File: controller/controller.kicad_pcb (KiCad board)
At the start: 2 copper layers, 241 parts, among them J1 CONN_01X10, J2 CONN_01X10, J3 CONN_01X10, J4 CONN_01X10, K1 RELAY_SEPARATED, K10 RELAY_SEPARATED, K11 RELAY_SEPARATED, K12 RELAY_SEPARATED, K13 RELAY_SEPARATED, K14 RELAY_SEPARATED, K15 RELAY_SEPARATED, K16 RELAY_SEPARATED, K17 RELAY_SEPARATED, K18 RELAY_SEPARATED, K19 RELAY_SEPARATED, K2 RELAY_SEPARATED, K20 RELAY_SEPARATED, K21 RELAY_SEPARATED, K22 RELAY_SEPARATED, K23 RELAY_SEPARATED, K24 RELAY_SEPARATED, K25 RELAY_SEPARATED, K26 RELAY_SEPARATED, K3 RELAY_SEPARATED, K4 RELAY_SEPARATED, K5 RELAY_SEPARATED, K6 RELAY_SEPARATED, K7 RELAY_SEPARATED, K8 RELAY_SEPARATED, K9 RELAY_SEPARATED, Q1 Q_NMOS_GSD, Q2 Q_NMOS_GSD, Q3 Q_PMOS_GSD, Q4 Q_NMOS_GSD, Q5 Q_PMOS_GSD, Q6 Q_PMOS_GSD, Q7 Q_NMOS_GSD, Q8 NDT2955, Q9 Q_NMOS_GSD, U1 OPTO-TRANSISTOR-4, U10 ULN2803A, U11 ULN2803A, U12 OPTO-TRANSISTOR-4, U2 ULN2801A, U3 SN65HVD72, U5 LM7805CT, U6 ULN2801A, U7 74LS04, U8 VNH3SP30, U9 74HC595

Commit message: Finish the routing, add some significant fixes: *correct to-252 pin numbering * longer pads for relays * fix footprint of the optocouplers
Also finish the routing
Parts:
- removed D40, D41: LED_Small_ALT, LEDs:LED_D5.0mm
- removed R27, R31, R32: R, Resistors_SMD:R_0603_HandSoldering
- added C45: 1u, Capacitors_SMD:C_0603_HandSoldering, B.Cu at (116.0, 95.0)
- added C46: C, Capacitors_SMD:C_0603_HandSoldering, B.Cu at (198.3, 130.1)
- added C47: 1u, Capacitors_SMD:C_1210_HandSoldering, B.Cu at (214.0, 143.5)
- added C48: 1u, Capacitors_SMD:C_0603, B.Cu at (145.2, 138.5)
- added J21: CONN_01X04, Connectors_JST:JST_EH_B04B-EH-A_04x2.50mm_Straight, F.Cu at (85.9, 159.6)
- added J22: BATT, Connectors_Terminal_Blocks:TerminalBlock_Pheonix_MKDS1.5-2pol, F.Cu at (65.4, 159.1)
- added J23: CONN_01X02, Connectors_Terminal_Blocks:TerminalBlock_Pheonix_MKDS1.5-2pol, F.Cu at (115.4, 157.6)
- added J24: CONN_01X02, Connectors_Terminal_Blocks:TerminalBlock_Pheonix_MKDS1.5-2pol, F.Cu at (273.9, 134.6)
- added J5: CONN_01X02, Connectors_Terminal_Blocks:TerminalBlock_Pheonix_MKDS1.5-2pol, F.Cu at (274.2, 151.2)
- added J6: CONN_01X05, Connectors_Terminal_Blocks:TerminalBlock_Pheonix_MKDS1.5-5pol, F.Cu at (145.4, 158.6)
- added J7: CONN_01X06, Socket_Strips:Socket_Strip_Straight_1x06_Pitch2.54mm, F.Cu at (147.9, 138.0)
- added R20: 0R05, TO_SOT_Packages_THT:TO-220-2_Vertical, F.Cu at (231.5, 144.5)
- added TP1: TEST, Measurement_Points:Measurement_Point_Round-TH_Small, F.Cu at (273.4, 94.1)
- added U13: LTV-814, Housings_DIP:DIP-4_W11.48mm_SMD, B.Cu at (265.5, 79.5)
- added U14: LTV-814, Housings_DIP:DIP-4_W11.48mm_SMD, B.Cu at (265.5, 98.6)
- added U15: LTV-814, Housings_DIP:DIP-4_W11.48mm_SMD, B.Cu at (265.5, 104.6)
- added U16: LM7805CT, TO_SOT_Packages_THT:TO-220_Vertical, F.Cu at (44.5, 116.5)
- added U4: LTV-814, Housings_DIP:DIP-4_W11.48mm_SMD, B.Cu at (245.9, 79.6)
- C16, C8: value C -> 1u
- C20, C21, C33, C35, C36, C38, C39, D16, D28, D34, D52, D53, D54, D56, D57, D58, Q1, Q2, Q3, Q4, Q5, Q6, Q7, Q8, Q9, R1, R10, R11, R12, R13, R14, R15, R16, R17, R18, R19, R2, R21, R22, R23, R24, R25, R26, R28, R29, R3, R30, R33, R4, R42, R43, R44, R45, R46, R47, R48, R49, R5, R50, R51, R52, R53, R54, R55, R56, R57, R58, R59, R6, R61, R62, R63, R64, R65, R66, R67, R68, R7, R8, R9, U3, U5, U8: moved to B.Cu
- C44: value C -> 1u; moved to B.Cu
- D30, D31, D32, D33, D51: footprint LEDs:LED_0805 -> LEDs:LED_D5.0mm
- D36: value LED_Small_ALT -> 5V; footprint LEDs:LED_D5.0mm -> Diodes_SMD:SOD-123; moved to B.Cu
- D55: footprint LEDs:LED_0603 -> LEDs:LED_D5.0mm
- J1, J2, J3, J4: footprint Connectors_Terminal_Blocks:TerminalBlock_Pheonix_MKDS1.5-10pol -> smalsiukas-footpints:TerminalBlock_5.08-10pol
- R60: footprint Resistors_SMD:R_0603 -> Resistors_SMD:R_0603_HandSoldering; moved to B.Cu
- RN1: value R_Network08 -> R_Pack08; footprint Resistors_THT:R_Array_SIP9 -> Resistors_SMD:R_Array_Convex_8x0602; moved to B.Cu
- RV1, RV2, RV3, RV4, RV5, RV6, RV7: footprint Potentiometers:Potentiometer_Trimmer_Bourns_3296P -> Potentiometers:Potentiometer_Trimmer_Bourns_3296W
- SH1: footprint w_conn_misc:arduino_nano_header -> SHIELD_ARDUINO:ARDUINO_NANO_2_CONTOUR_ELL
- U1, U12: value OPTO-TRANSISTOR-4 -> LTV-814; moved to B.Cu
- U7: value 74LS04 -> SN74AHCT1G14DBVR; moved to B.Cu
- U9: value 74HC595 -> 74HC595_WITH_PWR
- moved MK8 225.6 mm to (44.9, 43.6)
- moved R60 204.3 mm to (48.4, 138.1), turned to 90 degrees
- moved R61 196.9 mm to (54.4, 125.6)
- moved D52 191.8 mm to (51.9, 131.6), turned to 270 degrees
- moved D53 187.9 mm to (56.4, 131.6), turned to 270 degrees
- moved R62 178.6 mm to (75.2, 130.6)
- moved C39 177.7 mm to (73.4, 127.6)
- moved Q8 175.2 mm to (45.9, 130.6), turned to 90 degrees
- moved D55 173.4 mm to (78.0, 133.0), turned to 90 degrees
- moved MK5 173.3 mm to (43.9, 158.6)
- moved MK4 168.8 mm to (130.0, 160.0)
- moved SH1 167.8 mm to (132.1, 119.7), turned to 90 degrees
- moved D36 159.6 mm to (228.5, 147.8)
- moved U5 159.3 mm to (69.9, 134.6), turned to 270 degrees
- moved D34 159.3 mm to (55.9, 143.1)
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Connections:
- C1 pad 1: VCC -> /Power/+5V_DIRTY
- C10 pad 1: VCC -> /Power/+5V_DIRTY
- C11 pad 1: VCC -> /Power/+5V_DIRTY
- C12 pad 1: VCC -> /Power/+5V_DIRTY
- C13 pad 1: VCC -> /Power/+5V_DIRTY
- C14 pad 1: VCC -> /Power/+5V_DIRTY
- C15 pad 1: VCC -> /Power/+5V_DIRTY
- C16 pad 2: VCC -> /Power/+5V_DIRTY
- C17 pad 1: VCC -> /Power/+5V_DIRTY
- C18 pad 1: VCC -> /Power/+5V_DIRTY
- C19 pad 1: VCC -> /Power/+5V_DIRTY
- C2 pad 1: VCC -> /Power/+5V_DIRTY
- C21 pad 1: /Steering wheel feedback/WHEEL_POS_ANALOG -> /WHEEL_POS_ANALOG
- C22 pad 1: VCC -> /Power/+5V_DIRTY
- C23 pad 1: VCC -> /Power/+5V_DIRTY
- C24 pad 1: VCC -> /Power/+5V_DIRTY
- C25 pad 1: VCC -> /Power/+5V_DIRTY
- C26 pad 1: VCC -> /Power/+5V_DIRTY
- C27 pad 1: VCC -> /Power/+5V_DIRTY
- C28 pad 1: VCC -> /Power/+5V_DIRTY
- C29 pad 1: VCC -> /Power/+5V_DIRTY
- C3 pad 1: VCC -> /Power/+5V_DIRTY
- C30 pad 1: VCC -> /Power/+5V_DIRTY
- C31 pad 1: VCC -> /Power/+5V_DIRTY
- C32 pad 1: VCC -> /Power/+5V_DIRTY
- C33 pad 1: /Break H bridge/HBRIDGE_CURRENT_ANALOG -> /HBRIDGE_CURRENT_ANALOG
- C36 pad 1: VCC -> Net-(C36-Pad1)
- C4 pad 1: VCC -> /Power/+5V_DIRTY
- C42 pad 2: Net-(C42-Pad2) -> GND
- C43 pad 1: VCC -> /Power/+5V_DIRTY
- C44 pad 2: VCC -> /Power/+5V_DIRTY
- C5 pad 1: VCC -> /Power/+5V_DIRTY
- C6 pad 1: VCC -> /Power/+5V_DIRTY
- C7 pad 1: VCC -> /Power/+5V_DIRTY
- C8 pad 2: VCC -> /Power/+5V_DIRTY
- C9 pad 1: VCC -> /Power/+5V_DIRTY
- D1 pad 1: VCC -> /Power/+5V_DIRTY
- D10 pad 1: VCC -> /Power/+5V_DIRTY
- D11 pad 1: VCC -> /Power/+5V_DIRTY
- D12 pad 1: VCC -> /Power/+5V_DIRTY
- D13 pad 1: VCC -> /Power/+5V_DIRTY
- D14 pad 1: VCC -> /Power/+5V_DIRTY
- D15 pad 1: VCC -> /Power/+5V_DIRTY
- D16 pad 1: /Steering wheel feedback/WHEEL_POS_ANALOG -> /WHEEL_POS_ANALOG
- D17 pad 1: VCC -> /Power/+5V_DIRTY
- D18 pad 1: VCC -> /Power/+5V_DIRTY
- D19 pad 1: VCC -> /Power/+5V_DIRTY
- D2 pad 1: VCC -> /Power/+5V_DIRTY
- D20 pad 1: VCC -> /Power/+5V_DIRTY
- D21 pad 1: VCC -> /Power/+5V_DIRTY
- D22 pad 1: VCC -> /Power/+5V_DIRTY
- D23 pad 1: VCC -> /Power/+5V_DIRTY
- D24 pad 1: VCC -> /Power/+5V_DIRTY
- D25 pad 1: VCC -> /Power/+5V_DIRTY
- D26 pad 1: VCC -> /Power/+5V_DIRTY
- D27 pad 1: VCC -> /Power/+5V_DIRTY
- D28 pad 1: VCC -> /Power/+5V_DIRTY
- D29 pad 1: VCC -> /Power/+5V_DIRTY
- D3 pad 1: VCC -> /Power/+5V_DIRTY
- D34 pad 1: VCC -> Net-(C36-Pad1)
- D35 pad 1: /Control Switching/~GAZ_ENABLE_PWR -> /Control Switching/~KEY_ENABLE_PWR
- D36 pad 1: /Control Switching/~GAZ_SPEED1_PWR -> /HBRIDGE_CURRENT_ANALOG
- D36 pad 2: Net-(D36-Pad2) -> GND
- D37 pad 1: /Control Switching/~GAZ_SPEED2_PWR -> /Control Switching/~GAZ_SPEED3_PWR
- D38 pad 1: /Control Switching/~GAZ_SPEED3_PWR -> /Control Switching/~GAZ_SPEED2_PWR
- D39 pad 1: Net-(D39-Pad1) -> /Control Switching/~GAZ_SPEED1_PWR
- D4 pad 1: VCC -> /Power/+5V_DIRTY
- D42 pad 1: /Control Switching/~KEY_ENABLE_PWR -> /Control Switching/~GAZ_ENABLE_PWR
- D5 pad 1: VCC -> /Power/+5V_DIRTY
- D52 pad 1: Net-(D52-Pad1) -> VCC
- D56 pad 2: Net-(C42-Pad2) -> Net-(D56-Pad2)
- D58 pad 1: VCC -> /Power/+5V_DIRTY
- D6 pad 1: VCC -> /Power/+5V_DIRTY
- D7 pad 1: VCC -> /Power/+5V_DIRTY
- D8 pad 1: VCC -> /Power/+5V_DIRTY
- D9 pad 1: VCC -> /Power/+5V_DIRTY
- F2 pad 2: VCC -> Net-(C36-Pad1)
- K1 pad 1: VCC -> /Power/+5V_DIRTY
- K10 pad 1: VCC -> /Power/+5V_DIRTY
- K11 pad 1: VCC -> /Power/+5V_DIRTY
- K12 pad 1: VCC -> /Power/+5V_DIRTY
- K13 pad 1: VCC -> /Power/+5V_DIRTY
- K14 pad 1: VCC -> /Power/+5V_DIRTY
- K15 pad 1: VCC -> /Power/+5V_DIRTY
- K16 pad 10: VCC -> /Power/+5V_DIRTY
- K17 pad 10: VCC -> /Power/+5V_DIRTY
- K18 pad 1: VCC -> /Power/+5V_DIRTY
- K19 pad 1: VCC -> /Power/+5V_DIRTY
- K2 pad 1: VCC -> /Power/+5V_DIRTY
- K20 pad 1: VCC -> /Power/+5V_DIRTY
- K21 pad 1: VCC -> /Power/+5V_DIRTY
- K22 pad 1: VCC -> /Power/+5V_DIRTY
- K23 pad 10: VCC -> /Power/+5V_DIRTY
- K24 pad 10: VCC -> /Power/+5V_DIRTY
- K25 pad 10: VCC -> /Power/+5V_DIRTY
- K26 pad 10: VCC -> /Power/+5V_DIRTY
- K3 pad 1: VCC -> /Power/+5V_DIRTY
- K4 pad 1: VCC -> /Power/+5V_DIRTY
- K5 pad 1: VCC -> /Power/+5V_DIRTY
- K6 pad 1: VCC -> /Power/+5V_DIRTY
- K7 pad 1: VCC -> /Power/+5V_DIRTY
- K8 pad 1: VCC -> /Power/+5V_DIRTY
- K9 pad 1: VCC -> /Power/+5V_DIRTY
- Q3 pad 2: Net-(Q3-Pad2) -> /Takeover/GAZ_POT_WIPER_HACK
- Q5 pad 2: Net-(Q3-Pad2) -> /Takeover/GAZ_POT_WIPER_HACK
- Q6 pad 2: Net-(Q3-Pad2) -> /Takeover/GAZ_POT_WIPER_HACK
- Q7 pad 2: GND -> Net-(D56-Pad2)
- Q7 pad 3: Net-(C42-Pad2) -> GND
- Q8 pad 2: Net-(D52-Pad1) -> Net-(C36-Pad1)
- R12 pad 2: /Break H bridge/LINEAR_ACTUATOR_DIRECTION -> /LINEAR_ACTUATOR_ENABLE
- R13 pad 1: /Break H bridge/LINEAR_ACTUATOR_ENABLE -> /LINEAR_ACTUATOR_DIRECTION
- R14 pad 1: /Break H bridge/LINEAR_ACTUATOR_DIRECTION -> /LINEAR_ACTUATOR_ENABLE
- R15 pad 1: /Break H bridge/LINEAR_ACTUATOR_ENABLE -> /LINEAR_ACTUATOR_DIRECTION
- R16 pad 2: /Break H bridge/LINEAR_ACTUATOR_ENABLE -> /LINEAR_ACTUATOR_DIRECTION
- R18 pad 1: /Break H bridge/HBRIDGE_CURRENT_ANALOG -> /HBRIDGE_CURRENT_ANALOG
- R23 pad 2: /Control Switching/SPI_DATA -> /SPI_DATA
- R24 pad 2: /Control Switching/SPI_CLK -> /SPI_CLK
- R25 pad 2: /Control Switching/SPI_LATCH -> /SPI_LATCH
- R26 pad 1: VCC -> /Power/+5V_DIRTY
- R28 pad 1: VCC -> /Power/+5V_DIRTY
- R29 pad 1: VCC -> /Power/+5V_DIRTY
- R3 pad 1: Net-(Q3-Pad2) -> /Takeover/GAZ_POT_WIPER_HACK
- R30 pad 1: VCC -> /Power/+5V_DIRTY
- R33 pad 1: VCC -> /Power/+5V_DIRTY
- R34 pad 1: VCC -> /Power/+5V_DIRTY
- R35 pad 1: VCC -> /Power/+5V_DIRTY
- R36 pad 1: VCC -> /Power/+5V_DIRTY
- R37 pad 1: VCC -> /Power/+5V_DIRTY
- R38 pad 1: VCC -> /Power/+5V_DIRTY
- R39 pad 1: VCC -> /Power/+5V_DIRTY
- R40 pad 1: VCC -> /Power/+5V_DIRTY
- R41 pad 1: VCC -> /Power/+5V_DIRTY
- R5 pad 2: /Steering wheel feedback/WHEEL_POS_ANALOG -> /WHEEL_POS_ANALOG
- R57 pad 2: /RS485/RX -> Net-(R57-Pad2)
- R58 pad 1: /RS485/TX -> Net-(R58-Pad1)
- R59 pad 2: /RS485/~RE -> /~RE
- R6 pad 1: /Steering wheel feedback/WHEEL_POS_ANALOG -> /WHEEL_POS_ANALOG
- R61 pad 1: Net-(D52-Pad1) -> VCC
- R63 pad 2: /Stepper Interface/STEERING_ENABLE -> /STEERING_ENABLE
- R65 pad 2: /Stepper Interface/STEERING_DIR -> /STEERING_DIR
- R66 pad 2: /Stepper Interface/STEERING_STEP -> /STEERING_STEP
- R67 pad 1: /Stepper Interface/+5V -> +5V
- R68 pad 1: /Stepper Interface/+5V -> +5V
- R68 pad 2: /Stepper Interface/STEERING_FAULT -> /STEERING_FAULT
- RN1 pad 1: GND -> Net-(RN1-Pad1)
- RN1 pad 2: /Control Switching/KEY_ENABLE -> Net-(RN1-Pad2)
- RN1 pad 4: Net-(RN1-Pad4) -> /GAZ_SPEED1
- RN1 pad 5: Net-(RN1-Pad5) -> /GAZ_SPEED2
- RN1 pad 6: /Control Switching/GAZ_SPEED3 -> /GAZ_SPEED3
- RN1 pad 7: /Control Switching/GAZ_SPEED2 -> /Control Switching/GAZ_ENABLE
- RN1 pad 8: /Control Switching/GAZ_SPEED1 -> /Control Switching/KEY_ENABLE
- RN1 pad 9: /Control Switching/GAZ_ENABLE -> GND
- RV2 pad 1: /Takeover/GAZ_POT_V_HACK -> /Takeover/GAZ_POT_WIPER_HACK
- RV2 pad 2: Net-(Q5-Pad3) -> Net-(Q4-Pad3)
- RV2 pad 3: Net-(Q5-Pad3) -> Net-(Q4-Pad3)
- RV3 pad 1: Net-(Q3-Pad2) -> /Takeover/GAZ_POT_V_HACK
- RV3 pad 2: Net-(Q4-Pad3) -> Net-(Q5-Pad3)
- RV3 pad 3: Net-(Q4-Pad3) -> Net-(Q5-Pad3)
- RV4 pad 1: Net-(Q3-Pad2) -> /Takeover/GAZ_POT_WIPER_HACK
- RV6 pad 1: Net-(Q3-Pad2) -> /Takeover/GAZ_POT_WIPER_HACK
- RV7 pad 2: Net-(Q3-Pad2) -> /Takeover/GAZ_POT_WIPER_HACK
- RV7 pad 3: Net-(Q3-Pad2) -> /Takeover/GAZ_POT_WIPER_HACK
- SH1 pad 1: Net-(SH1-Pad1) -> /RS485/TX
- SH1 pad 3: Net-(SH1-Pad3) -> /Break H bridge/MAGNET_ENGAGE
- U1 pad 1: VCC -> /Power/+5V_DIRTY
- U1 pad 2: Net-(R9-Pad1) -> Net-(R42-Pad1)
- U1 pad 3: VCC -> Net-(R43-Pad1)
- U1 pad 4: Net-(R7-Pad1) -> /Takeover/GAZ_POT_V_HACK
- U10 pad 1: /Control Switching/GAZ_ENABLE -> /Control Switching/KEY_ENABLE
- U10 pad 10: VCC -> /Power/+5V_DIRTY
- U10 pad 11: /Control Switching/~KEY_ENABLE_PWR -> Net-(U10-Pad11)
- U10 pad 14: Net-(D39-Pad1) -> /Control Switching/~GAZ_SPEED1_PWR
- U10 pad 15: /Control Switching/~GAZ_SPEED3_PWR -> /Control Switching/~GAZ_SPEED2_PWR
- U10 pad 16: /Control Switching/~GAZ_SPEED2_PWR -> /Control Switching/~GAZ_SPEED3_PWR
- U10 pad 17: /Control Switching/~GAZ_SPEED1_PWR -> /Control Switching/~GAZ_ENABLE_PWR
- U10 pad 18: /Control Switching/~GAZ_ENABLE_PWR -> /Control Switching/~KEY_ENABLE_PWR
- U10 pad 2: /Control Switching/GAZ_SPEED1 -> /Control Switching/GAZ_ENABLE
- U10 pad 3: /Control Switching/GAZ_SPEED2 -> /GAZ_SPEED3
- U10 pad 4: /Control Switching/GAZ_SPEED3 -> /GAZ_SPEED2
- U10 pad 5: Net-(RN1-Pad5) -> /GAZ_SPEED1
- U10 pad 6: Net-(RN1-Pad4) -> Net-(RN1-Pad3)
- U10 pad 7: Net-(RN1-Pad3) -> Net-(RN1-Pad2)
- U10 pad 8: /Control Switching/KEY_ENABLE -> Net-(RN1-Pad1)
- U11 pad 10: VCC -> /Power/+5V_DIRTY
- U12 pad 1: VCC -> /Power/+5V_DIRTY
- U12 pad 2: Net-(R42-Pad1) -> Net-(R48-Pad1)
- U12 pad 3: VCC -> Net-(R49-Pad1)
- U12 pad 4: Net-(R8-Pad1) -> /Takeover/GAZ_POT_V_HACK
- U2 pad 10: VCC -> /Power/+5V_DIRTY
- U2 pad 11: Net-(C9-Pad2) -> Net-(C12-Pad2)
- U2 pad 12: Net-(C10-Pad2) -> Net-(C11-Pad2)
- U2 pad 13: Net-(C11-Pad2) -> Net-(C10-Pad2)
- U2 pad 14: Net-(C12-Pad2) -> Net-(C9-Pad2)
- U3 pad 1: /RS485/RX -> Net-(R57-Pad2)
- U3 pad 2: /RS485/~RE -> /~RE
- U3 pad 3: /RS485/~RE -> /~RE
- U3 pad 4: /RS485/TX -> Net-(R58-Pad1)
- U6 pad 10: VCC -> /Power/+5V_DIRTY
- U7 pad 1: Net-(R12-Pad1) -> (no net)
- U7 pad 2: Net-(U7-Pad2) -> Net-(R12-Pad1)
- U7 pad 3: (no net) -> GND
- U7 pad 4: (no net) -> Net-(U7-Pad4)
- U7 pad 5: (no net) -> +5V
- U8 pad 5: Net-(U7-Pad2) -> Net-(U7-Pad4)
- U9 pad 16: VCC -> +5V
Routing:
- net /Power/+5V_DIRTY: track 0.00 -> 842.6 mm, vias 0 -> 8
- net +5V: track 0.00 -> 321.9 mm, vias 0 -> 4
- net /Takeover/GAZ_POT_WIPER_HACK: track 0.00 -> 210.7 mm, vias 0 -> 7
- net /Takeover/TAKEOVER: track 8.89 -> 183.3 mm, vias 0 -> 7
- net /Break H bridge/MAGNET_ENGAGE: track 0.00 -> 142.2 mm, vias 0 -> 5
- net /Takeover/GAZ_POT_GND_HACK: track 0.00 -> 133.5 mm
- net /Takeover/GAZ_POT_V_HACK: track 0.00 -> 132.4 mm, vias 0 -> 4
- net /HBRIDGE_CURRENT_ANALOG: track 0.00 -> 124.3 mm, vias 0 -> 4
- net Net-(C40-Pad2): track 0.00 -> 110.5 mm
- net /GAZ_SPEED3: track 0.00 -> 100.9 mm, vias 0 -> 2
- net /Control Switching/GAZ_ENABLE: track 0.00 -> 100.2 mm, vias 0 -> 2
- net /GAZ_SPEED2: track 0.00 -> 99.0 mm, vias 0 -> 2
- net /Control Switching/KEY_ENABLE: track 0.00 -> 98.8 mm, vias 0 -> 2
- net /GAZ_SPEED1: track 0.00 -> 97.7 mm, vias 0 -> 2
- net Net-(C40-Pad1): track 0.00 -> 92.1 mm
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- added copper zone on B.Cu, net GND
- added copper zone on F.Cu, net GND
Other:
- board outline added: 240 x 125 mm
- net class Default: trace_width 0.8 -> 0.6
- board text added: "TODO: sutvarkyti 2 ir 5 pinų terminalų footprintus"

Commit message: Update the 5 and 2 pin terminal footprints, shuffle around some tracks
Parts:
- J22, J23, J24, J5: footprint Connectors_Terminal_Blocks:TerminalBlock_Pheonix_MKDS1.5-2pol -> smalsiukas-footpints:TerminalBlock_5.08-2pol
- J6: footprint Connectors_Terminal_Blocks:TerminalBlock_Pheonix_MKDS1.5-5pol -> smalsiukas-footpints:TerminalBlock_5.08-5pol
- moved J6 20.0 mm to (165.0, 154.6), turned to 180 degrees
- moved J22 7.18 mm to (71.0, 154.6), turned to 180 degrees
- moved J5 6.56 mm to (270.2, 146.0), turned to 270 degrees
- moved J23 6.35 mm to (121.0, 154.6), turned to 180 degrees
- moved J24 6.09 mm to (270.0, 129.9), turned to 270 degrees
- moved Q9 5.96 mm to (150.3, 148.7)
- moved R63 5.96 mm to (150.3, 143.7)
- moved R64 5.96 mm to (150.3, 145.2)
- moved R67 5.96 mm to (147.3, 150.2)
- moved C47 4.22 mm to (210.1, 145.1)
- moved R54 4.00 mm to (255.6, 151.2)
- moved C33 4.00 mm to (224.0, 146.0)
- moved C40 4.00 mm to (247.9, 136.6)
- moved C41 4.00 mm to (230.9, 136.6)
- moved C42 4.00 mm to (245.9, 146.1)
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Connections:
- J22 pad 1: Net-(F2-Pad1) -> GND
- J22 pad 2: GND -> Net-(F2-Pad1)
- J24 pad 1: Net-(C40-Pad1) -> Net-(C40-Pad2)
- J24 pad 2: Net-(C40-Pad2) -> Net-(C40-Pad1)
- J5 pad 1: Net-(D56-Pad2) -> VCC
- J5 pad 2: VCC -> Net-(D56-Pad2)
- J6 pad 1: /Stepper Interface/GECKO_DISABLE -> GND
- J6 pad 2: /STEERING_FAULT -> /Stepper Interface/GECKO_STEP
- J6 pad 4: /Stepper Interface/GECKO_STEP -> /STEERING_FAULT
- J6 pad 5: GND -> /Stepper Interface/GECKO_DISABLE
- R5 pad 1: Net-(J23-Pad1) -> Net-(J23-Pad2)
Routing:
- net /WHEEL_POS_ANALOG: track 47.0 -> 97.8 mm, vias 2 -> 4
- net Net-(C40-Pad1): track 92.1 -> 105.0 mm, vias 0 -> 2
- net VCC: track 395.1 -> 386.8 mm
- net /HBRIDGE_CURRENT_ANALOG: track 124.3 -> 119.1 mm
- net /Takeover/SEAT_GND_OUT: track 8.91 -> 14.0 mm
- net /Takeover/PARKING_OUT: track 7.84 -> 12.9 mm
- net /Takeover/MIRGALKE_OUT: track 10.5 -> 15.6 mm
- net /Takeover/LIGHTS_OUT: track 8.43 -> 13.5 mm
- net /Takeover/KEY_HOT_OUT: track 8.49 -> 13.6 mm
- net /Takeover/KEY_COLD_OUT: track 8.49 -> 13.6 mm
- net /Takeover/HORN_SW_OUT: track 7.91 -> 13.0 mm
- net /Takeover/GAZ_SW_NO_OUT: track 8.54 -> 13.6 mm
- net /Takeover/GAZ_SW_NC_OUT: track 8.54 -> 13.6 mm
- net /Takeover/GAZ_SW_COMMON: track 41.2 -> 46.3 mm
- net /Takeover/GAZ_POT_WIPER_OUT: track 8.49 -> 13.6 mm
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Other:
- board text removed: "TODO: sutvarkyti 2 ir 5 pinų terminalų footprintus"

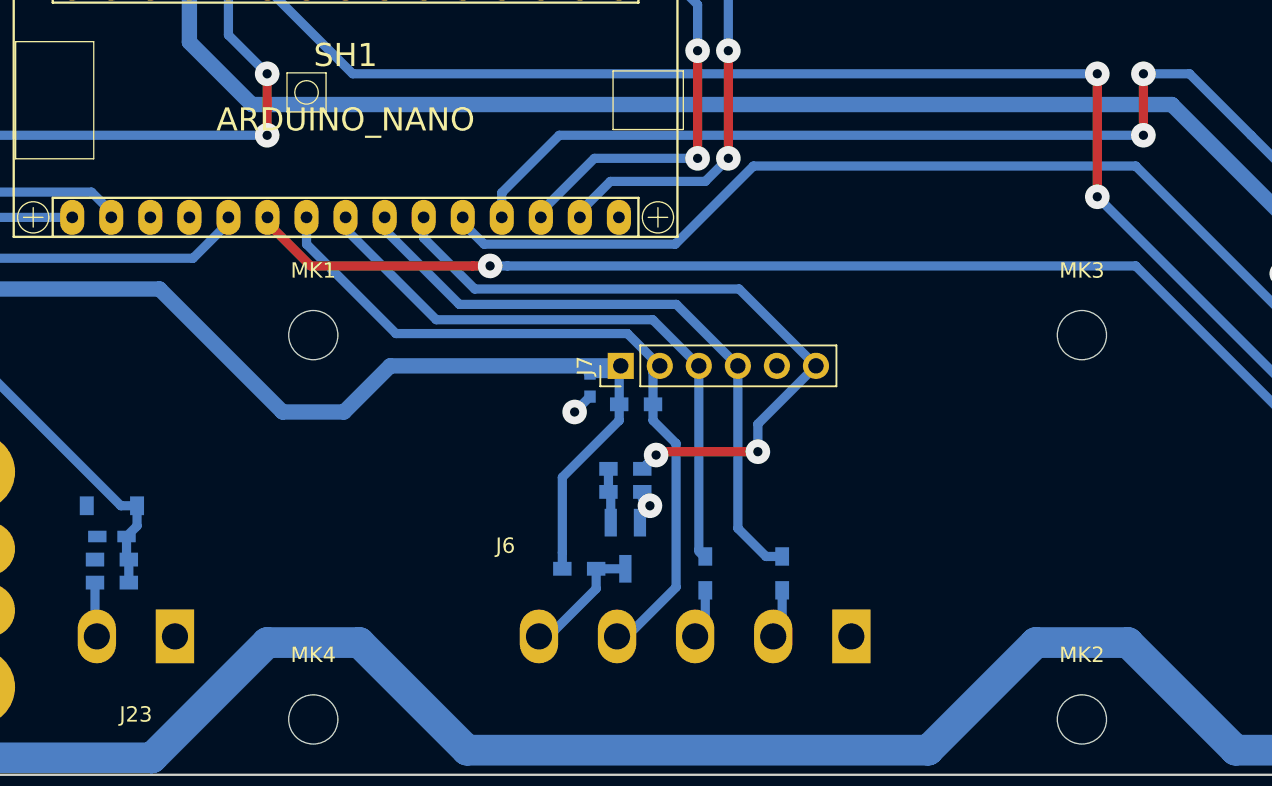
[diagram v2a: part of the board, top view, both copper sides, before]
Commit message: send controller and line interface boards for manufacturing
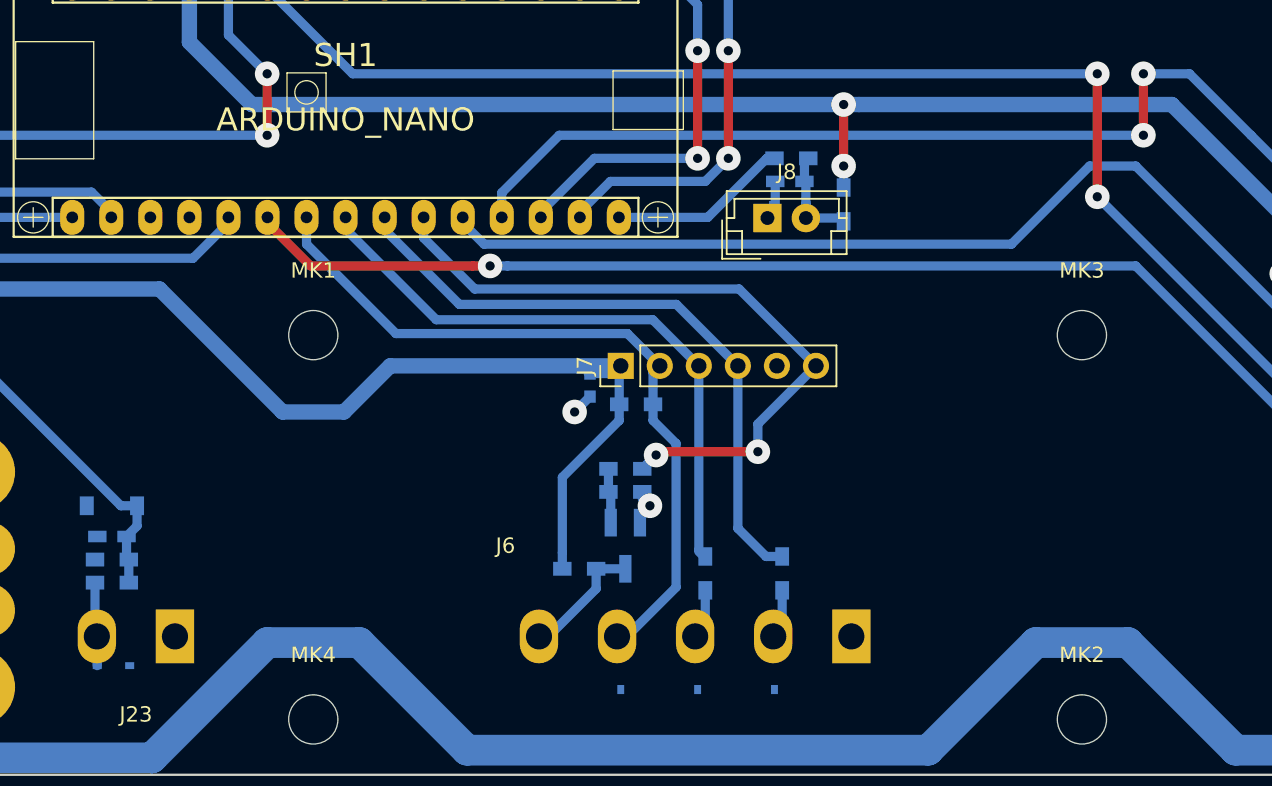
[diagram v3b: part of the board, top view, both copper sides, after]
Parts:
- added C49: C, Capacitors_SMD:C_0603_HandSoldering, B.Cu at (161.0, 125.0)
- added D40: D_TVS_ALT, Diodes_SMD:SOD-323, B.Cu at (161.0, 126.5)
- added D41: D_TVS_ALT, Diodes_SMD:SOD-323, B.Cu at (117.0, 156.5)
- added D59: D_TVS_ALT, Diodes_SMD:SOD-323, B.Cu at (155.0, 157.0)
- added D60: D_TVS_ALT, Diodes_SMD:SOD-323, B.Cu at (160.0, 157.0)
- added D61: D_TVS_ALT, Diodes_SMD:SOD-323, B.Cu at (150.0, 157.0)
- added J8: CONN_01X02, Connectors_JST:JST_EH_B02B-EH-A_02x2.50mm_Straight, F.Cu at (159.5, 127.4)
- added R27: R, Resistors_SMD:R_0603_HandSoldering, B.Cu at (164.5, 126.5)
- added R31: R, Resistors_SMD:R_0603_HandSoldering, B.Cu at (161.1, 123.5)
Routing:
- net Net-(R31-Pad1): track 0.00 -> 11.7 mm
- net Net-(C49-Pad1): track 0.00 -> 7.46 mm
- net +5V: track 319.5 -> 325.9 mm, vias 2 -> 4
- net GND: track 58.1 -> 60.6 mm
- net Net-(D41-Pad1): track 3.67 -> 5.58 mm

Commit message: Various fixes and comments to the controller board, also making it suitable for non-plated holes.
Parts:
- removed RN1, RN2: R_Pack08, Resistors_SMD:R_Array_Convex_8x0602
- added R32: R, Resistors_SMD:R_0603_HandSoldering, B.Cu at (214.7, 78.6)
- added R69: R, Resistors_SMD:R_0603_HandSoldering, B.Cu at (214.7, 80.1)
- added R70: R, Resistors_SMD:R_0603_HandSoldering, B.Cu at (131.7, 74.2)
- added R71: R, Resistors_SMD:R_0603_HandSoldering, B.Cu at (214.7, 81.6)
- added R72: R, Resistors_SMD:R_0603_HandSoldering, B.Cu at (131.7, 75.7)
- added R73: R, Resistors_SMD:R_0603_HandSoldering, B.Cu at (214.7, 83.1)
- added R74: R, Resistors_SMD:R_0603_HandSoldering, B.Cu at (131.7, 77.2)
- added R75: R, Resistors_SMD:R_0603_HandSoldering, B.Cu at (214.7, 84.6)
- added R76: R, Resistors_SMD:R_0603_HandSoldering, B.Cu at (131.7, 78.7)
- added R77: R, Resistors_SMD:R_0603_HandSoldering, B.Cu at (214.7, 86.1)
- added R78: R, Resistors_SMD:R_0603_HandSoldering, B.Cu at (131.7, 80.2)
- added R79: R, Resistors_SMD:R_0603_HandSoldering, B.Cu at (214.7, 87.6)
- added R80: R, Resistors_SMD:R_0603_HandSoldering, B.Cu at (131.7, 81.7)
- added R81: R, Resistors_SMD:R_0603_HandSoldering, B.Cu at (214.7, 89.1)
- added R82: R, Resistors_SMD:R_0603_HandSoldering, B.Cu at (131.7, 83.2)
- added R83: R, Resistors_SMD:R_0603_HandSoldering, B.Cu at (131.7, 84.7)
- C8: moved to B.Cu
- moved C8 8.52 mm to (261.0, 55.8), turned to 270 degrees
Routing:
- net GND: track 60.6 -> 144.1 mm, vias 28 -> 45
- net /Power/+5V_DIRTY: track 842.6 -> 916.3 mm, vias 8 -> 38
- net /GAZ_SPEED1: track 97.7 -> 113.6 mm
- net /GAZ_SPEED2: track 99.0 -> 114.2 mm
- net /Control Switching/GAZ_ENABLE: track 100.2 -> 114.1 mm
- net /GAZ_SPEED3: track 100.9 -> 114.2 mm
- net /Control Switching/KEY_ENABLE: track 98.8 -> 111.2 mm
- net /ControlHacks/LIGHTS_COMMON: track 52.9 -> 63.1 mm
- net /Takeover/GAZ_POT_WIPER_HACK: track 210.7 -> 218.7 mm, vias 7 -> 8
- net /Control Switching/~GAZ_SPEED2_PWR: track 91.2 -> 98.3 mm
- net /Control Switching/~GAZ_SPEED1_PWR: track 81.4 -> 88.5 mm
- net /Takeover/TAKEOVER: track 183.3 -> 189.7 mm
- net /Control Switching/~GAZ_SPEED3_PWR: track 62.4 -> 68.1 mm
- net Net-(R77-Pad2): track 3.63 -> 9.08 mm
- net /ControlHacks/AUX_COMMON: track 31.8 -> 36.8 mm
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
